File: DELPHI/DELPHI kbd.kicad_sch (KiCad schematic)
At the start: 86 parts, among them SW1 SW_Push_45deg, SW10 SW_Push_45deg, SW11 SW_Push_45deg, SW12 SW_Push_45deg, SW13 SW_Push_45deg, SW14 SW_Push_45deg, SW15 SW_Push_45deg, SW16 SW_Push_45deg, SW17 SW_Push_45deg, SW18 SW_Push_45deg, SW19 SW_Push_45deg, SW2 SW_Push_45deg, SW20 SW_Push_45deg, SW21 SW_Push_45deg, SW22 SW_Push_45deg, SW23 SW_Push_45deg, SW24 SW_Push_45deg, SW25 SW_Push_45deg, SW26 SW_Push_45deg, SW27 SW_Push_45deg, SW28 SW_Push_45deg, SW29 SW_Push_45deg, SW3 SW_Push_45deg, SW30 SW_Push_45deg, SW31 SW_Push_45deg, SW32 SW_Push_45deg, SW33 SW_Push_45deg, SW34 SW_Push_45deg, SW35 SW_Push_45deg, SW36 SW_Push_45deg, SW37 SW_Push_45deg, SW38 SW_Push_45deg, SW39 SW_Push_45deg, SW4 SW_Push_45deg, SW40 SW_Push_45deg, SW41 SW_Push_45deg, SW42 SW_Push_45deg, SW5 SW_Push_45deg, SW6 SW_Push_45deg, SW7 SW_Push_45deg, SW8 SW_Push_45deg, SW9 SW_Push_45deg, U1 QTPy, U2 QTPy

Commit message: Update KiCAD files (specifically the schematic)
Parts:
- SW1, SW10, SW11, SW12, SW13, SW14, SW15, SW16, SW17, SW18, SW19, SW2, SW20, SW21, SW22, SW23, SW24, SW25, SW26, SW27, SW28, SW29, SW3, SW30, SW31, SW32, SW33, SW34, SW35, SW36, SW37, SW38, SW39, SW4, SW40, SW41, SW42, SW5, SW6, SW7, SW8, SW9: footprint keyswitches:Kailh_socket_PG1350 -> keyswitches.pretty-2:Kailh_socket_PG1350
- U1, U2: value QTPy -> Adafruit QT Py RP2040; footprint Seeeduino XIAO KICAD:Seeeduino XIAO-MOUDLE14P-2.54-21X17.8MM -> Mech Keys:Adafruit QT Py RP2040; symbol Seeeduino XIAO:SeeeduinoXIAO -> Mech Keys:Adafruit_QT_Py_RP2040
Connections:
- no-connect marks 18 -> 6
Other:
- note added: ""STEMMA QT" cable connection (off-board; external part)"
- note added: "LEFT MCU"
- note added: "RIGHT MCU"
- moved on the sheet: D22, D23, D24, D25, D26, D27, D28, D29, D30, D31, D32, D33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

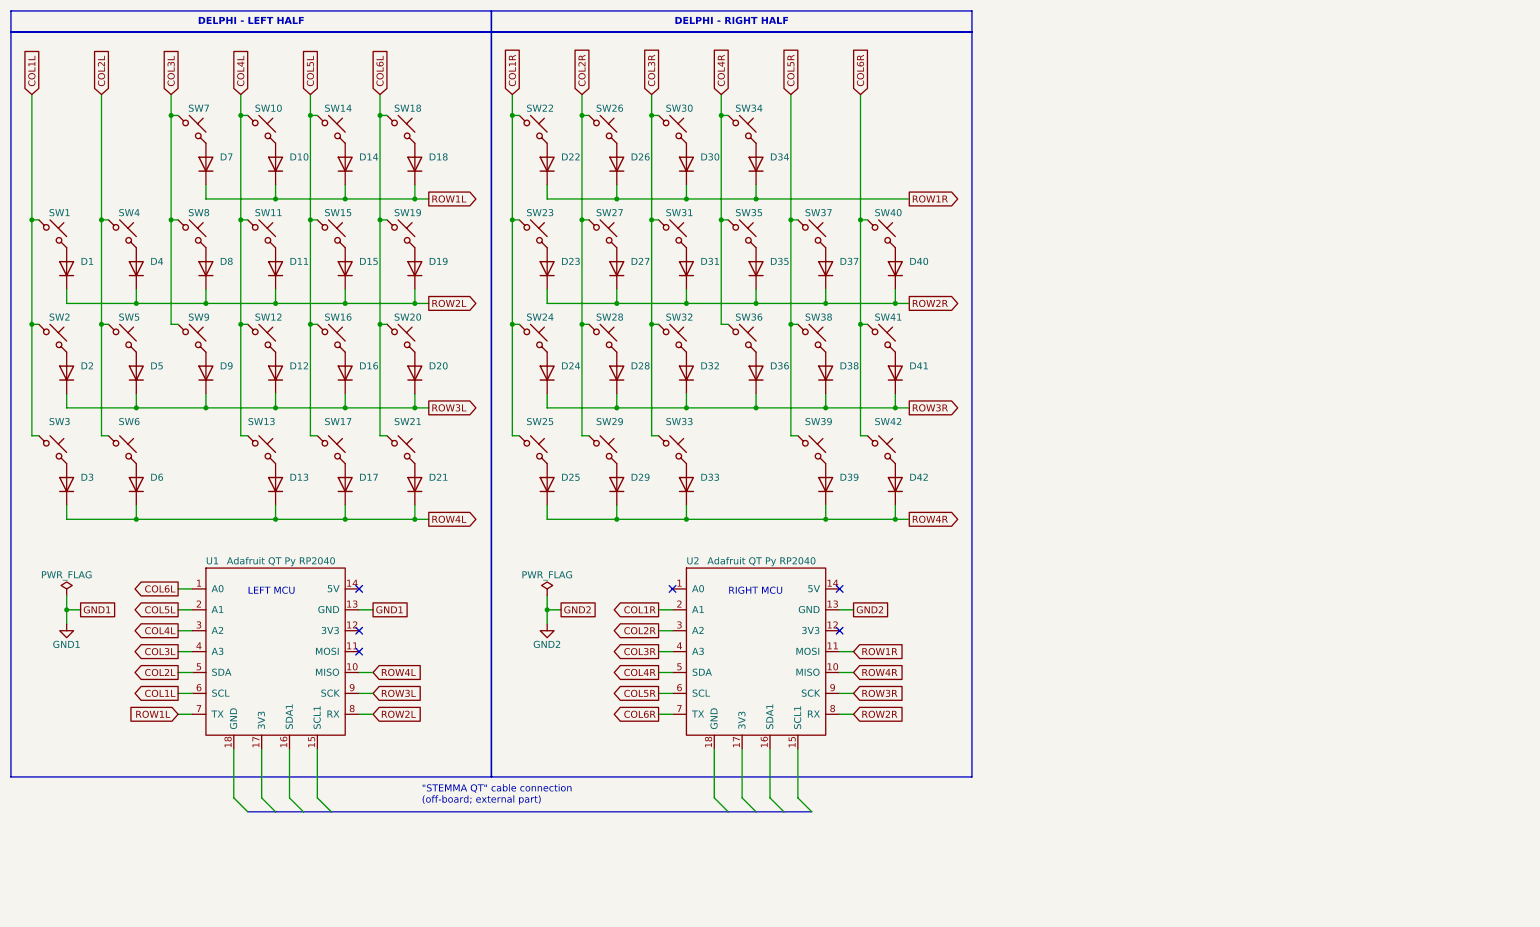
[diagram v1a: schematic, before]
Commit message: Update project files for 1.0.2 revision
Change mounting holes to accommodate PEM P/N: SMTSOB-M2-6ET (M2x6mm SMT standoff); update diode P/N to 1N4148W; clean up silkscreen placement
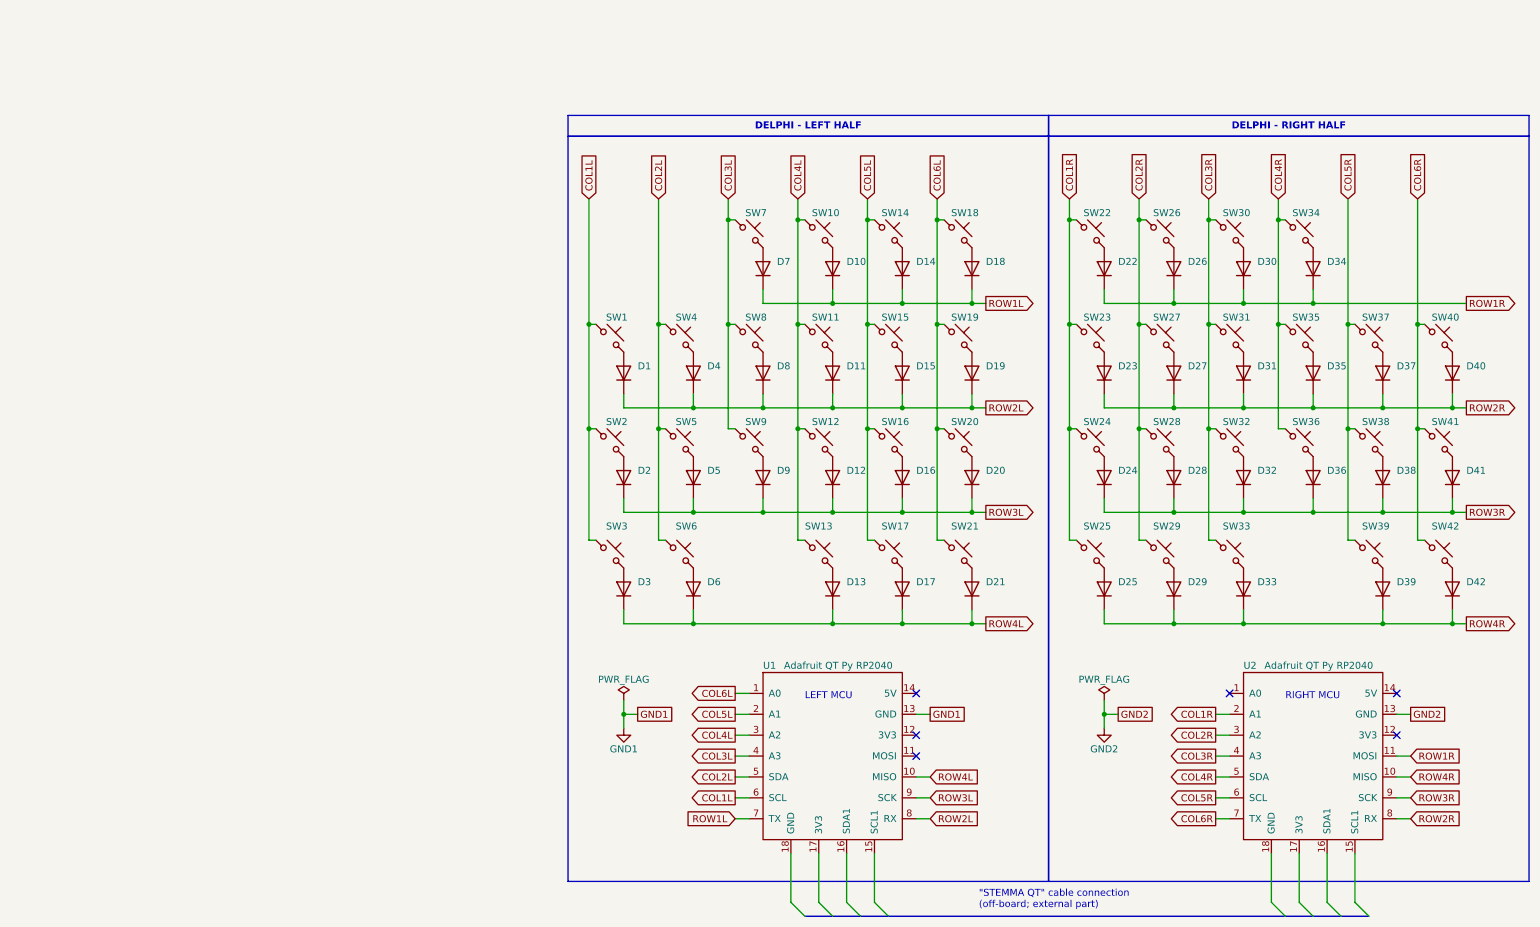
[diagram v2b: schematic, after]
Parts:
- D1, D10, D11, D12, D13, D14, D15, D16, D17, D18, D19, D2, D20, D21, D22, D23, D24, D25, D26, D27, D28, D29, D3, D30, D31, D32, D33, D34, D35, D36, D37, D38, D39, D4, D40, D41, D42, D5, D6, D7, D8, D9: value 1N4448WT -> 1N4148W; symbol Diode:1N4448WT -> Diode:1N4148W
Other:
- moved on the sheet: D1, D10, D11, D12, D13, D14, D15, D16, D17, D18, D19, D2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
